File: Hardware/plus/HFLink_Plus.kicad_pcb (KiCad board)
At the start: 4 copper layers, 48.5 x 33.5 mm, 123 parts, among them J1 DF40C-60DS-0.4V(51), J2 DF40C-60DS-0.4V(51), J3 Conn_ARM_JTAG_SWD_20, J4 USB_C_Receptacle_USB2.0_16P, J5 WAFER-ZH1.5-4PWB, J6 Conn_01x08_Pin, Q1 SI2305, U1 ECMF02-2AMX6, U10 SN74LVC1G125DCK, U11 SN74LVC1G125DCK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

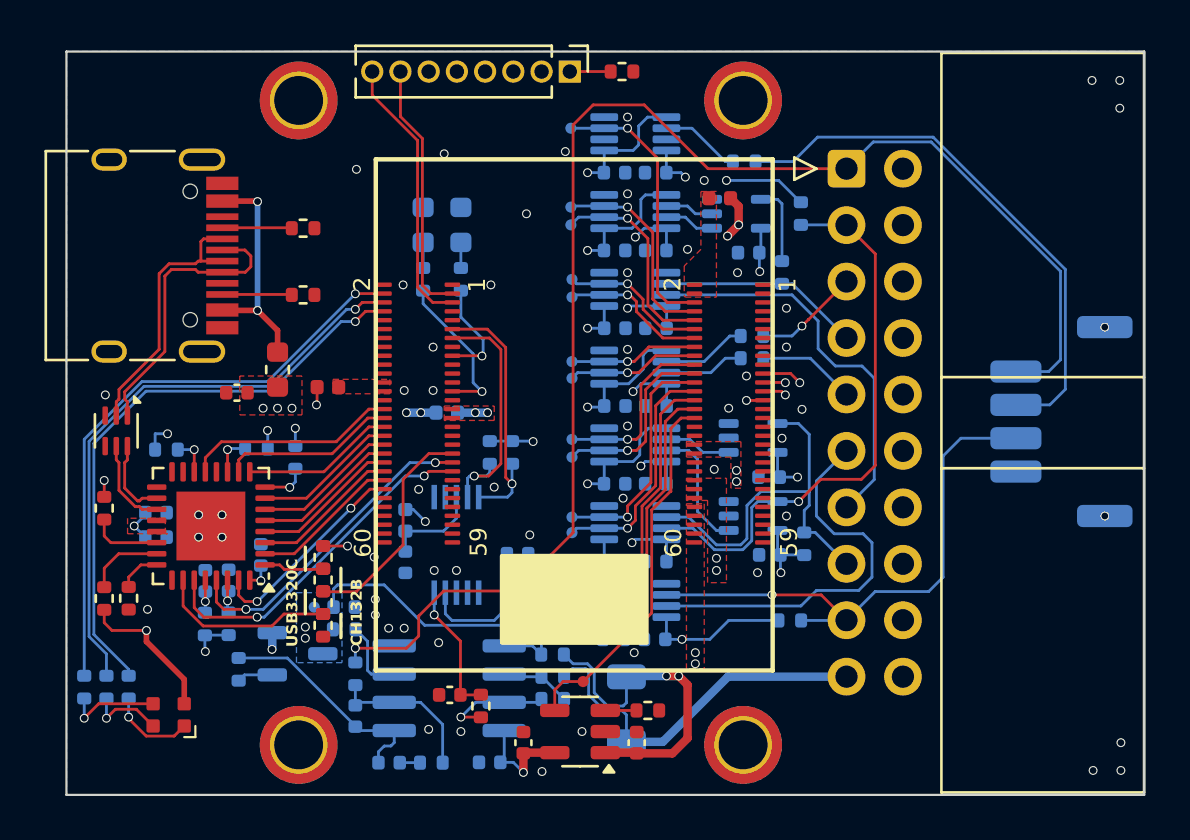
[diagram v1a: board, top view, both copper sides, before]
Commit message: [PCB] vtrg增加100K下拉电阻
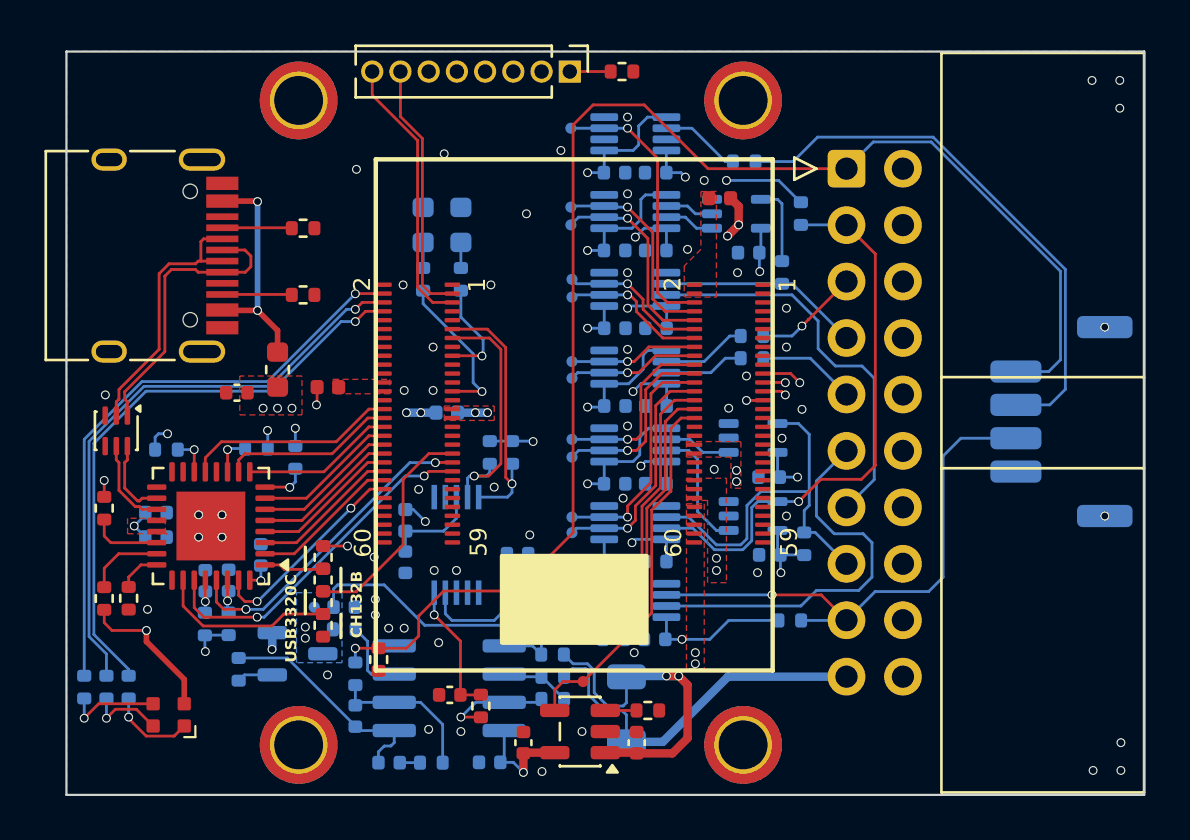
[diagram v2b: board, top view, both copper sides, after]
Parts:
- added R43: 100K,1%, Resistor_SMD:R_0402_1005Metric, F.Cu at (74.5, 84.9)
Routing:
- net GND: vias 59 -> 60

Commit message: PCB JTAG每个信号都增加33欧串阻，USB供电电压传感
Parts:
- added C33: 2.2nF,50V, Capacitor_SMD:C_0402_1005Metric, B.Cu at (74.0, 75.3)
- added R44: 33R,1%, Resistor_SMD:R_0402_1005Metric, B.Cu at (89.9, 82.8)
- added R45: 33R,1%, Resistor_SMD:R_0402_1005Metric, B.Cu at (89.9, 81.8)
- added R46: 33R,1%, Resistor_SMD:R_0402_1005Metric, B.Cu at (90.4, 68.8)
- added R47: 10K,1%, Resistor_SMD:R_0402_1005Metric, B.Cu at (74.0, 73.3)
- added R48: 10K,1%, Resistor_SMD:R_0402_1005Metric, B.Cu at (74.0, 74.3)
- moved R7 0.69 mm to (93.2, 68.0), turned to 0 degrees
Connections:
- R7 pad 1: Net-(R7-Pad1) -> Net-(U4-B2)
- U12 pad 6: /INTERFACE/UART_RX -> Net-(U12-B2)
- U12 pad 7: /INTERFACE/RTCK -> Net-(U12-B1)
- U14 pad 6: unconnected-(U14-AIN2-Pad6) -> /INTERFACE/VBUS_ADC
- U3 pad 4: Net-(R7-Pad1) -> Net-(U4-B2)
- U4 pad 6: /INTERFACE/TMS -> Net-(U4-B2)
- U4 pad 7: /INTERFACE/TDO -> Net-(U4-B1)
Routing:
- net Net-(U4-B2): track 0.00 -> 9.81 mm
- net /INTERFACE/VBUS_ADC: track 0.00 -> 7.37 mm
- net /INTERFACE/TMS: track 9.11 -> 3.24 mm
- net Net-(R7-Pad1): track 3.61 -> 0.00 mm
- net /INTERFACE/TDO: track 18.0 -> 14.5 mm
- net +5V: track 58.8 -> 62.2 mm
- net /INTERFACE/UART_RX: track 24.8 -> 22.0 mm
- net /INTERFACE/RTCK: track 17.8 -> 15.0 mm
- net Net-(U4-B1): track 0.00 -> 2.49 mm
- net Net-(U12-B2): track 0.00 -> 1.99 mm
- net Net-(U12-B1): track 0.00 -> 1.99 mm
- net GND: vias 60 -> 62
